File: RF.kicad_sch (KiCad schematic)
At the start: 28 parts, among them J1 Conn_Coaxial, SW1 SW_DIP_x01, U1 AD8307, U2 L7805

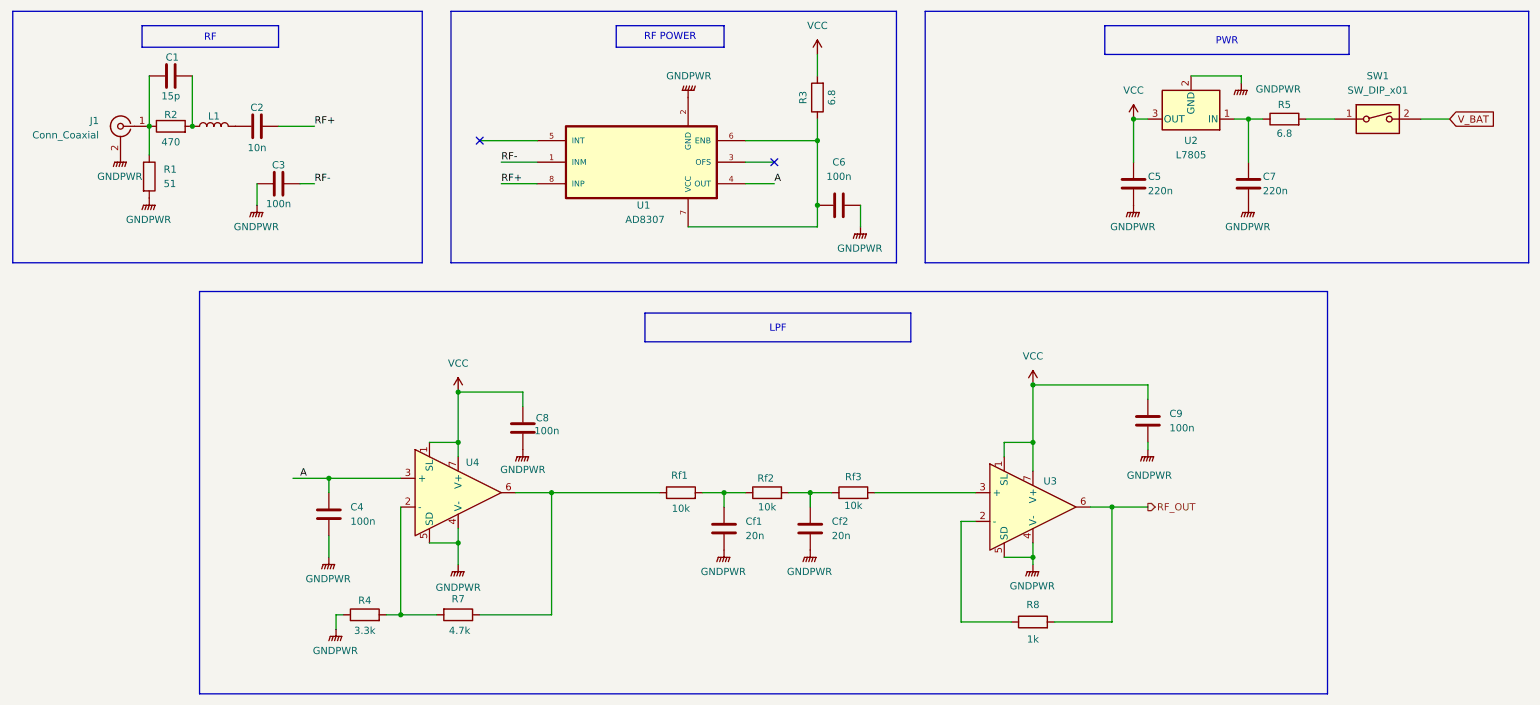
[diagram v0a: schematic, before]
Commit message: dodane C10
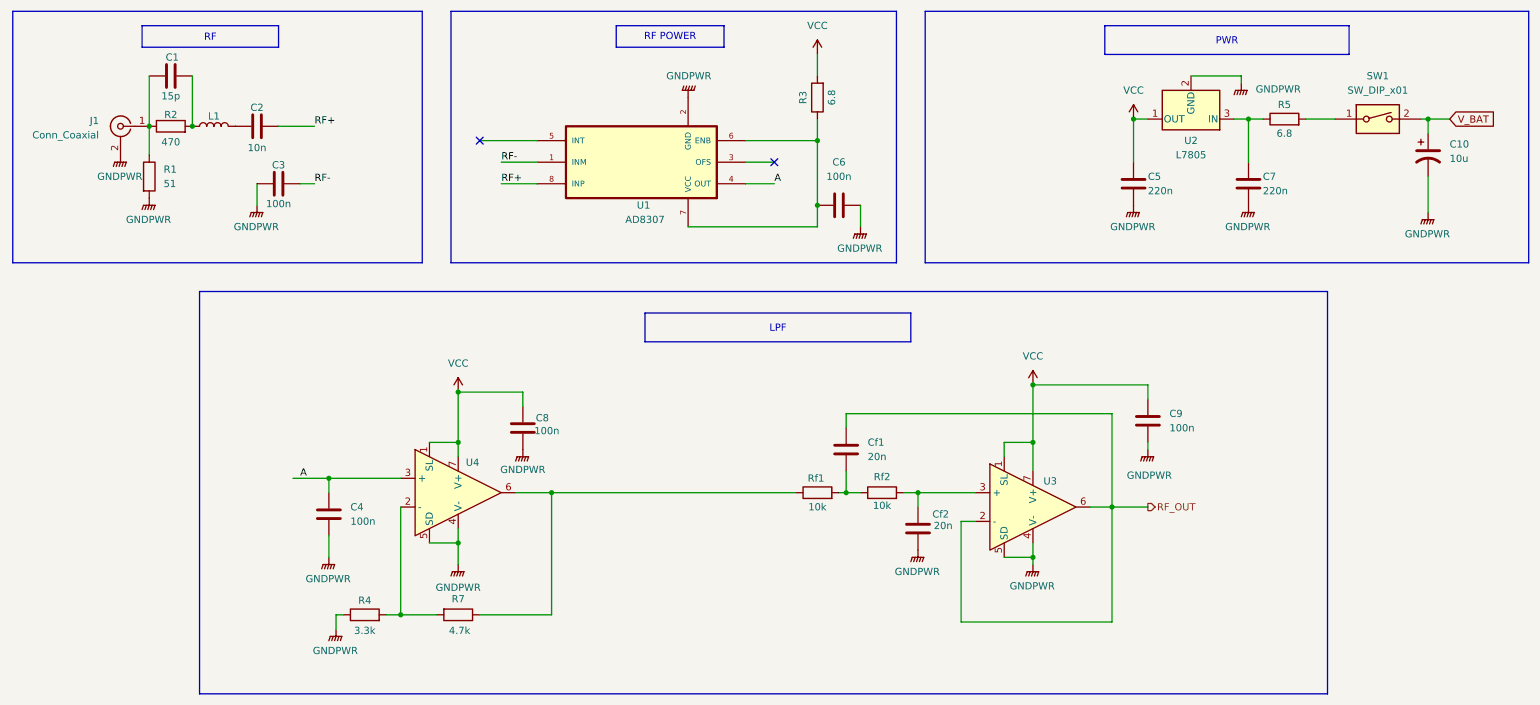
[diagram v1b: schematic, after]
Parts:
- removed R8: 1k, Resistor_SMD:R_1206_3216Metric_Pad1.30x1.75mm_HandSolder, symbol Device:R
- removed Rf1: 10k, Resistor_SMD:R_1206_3216Metric_Pad1.30x1.75mm_HandSolder, symbol Device:R
- added C10: 10u, Capacitor_SMD:CP_Elec_6.3x5.3, symbol Device:C_Polarized_US
- U2: footprint Package_TO_SOT_THT:TO-220-3_Horizontal_TabDown -> Package_TO_SOT_SMD:SOT-89-3_Handsoldering
- renumbered Rf2 to Rf1, Rf3 to Rf2
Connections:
- net GNDPWR: now also C10.2; no longer Cf1.2
- net RF_OUT: now also Cf1.1, U3.2 (-)
- net VCC: now also U2.1 (OUT); no longer U2.3 (OUT)
- net V_BAT: now also C10.1
- net at C7.1, R5.1: now also U2.3 (IN); no longer U2.1 (IN)
- net at Rf1.2, Rf2.1: now also Cf1.2; no longer Cf2.1
- net at R7.1, U4.6: now also Rf1.1
- net at Rf2.2, U3.3 (+): now also Cf2.1
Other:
- moved on the sheet: Cf1, Cf2, Rf1, Rf2
